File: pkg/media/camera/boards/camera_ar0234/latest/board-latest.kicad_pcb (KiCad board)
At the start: 6 copper layers, 32 x 32 mm, 69 parts, among them J1 FH34SRJ-22S-0.5SH_50_, Q1 BSS138, Q2 BSS138, U2 ATtiny402-SS, U3 LP5907MFX-2.8, U4 TLV74318PDBVR, U5 TLV75512PDYDR, X1 ECS-2520MV-240-DN-TR

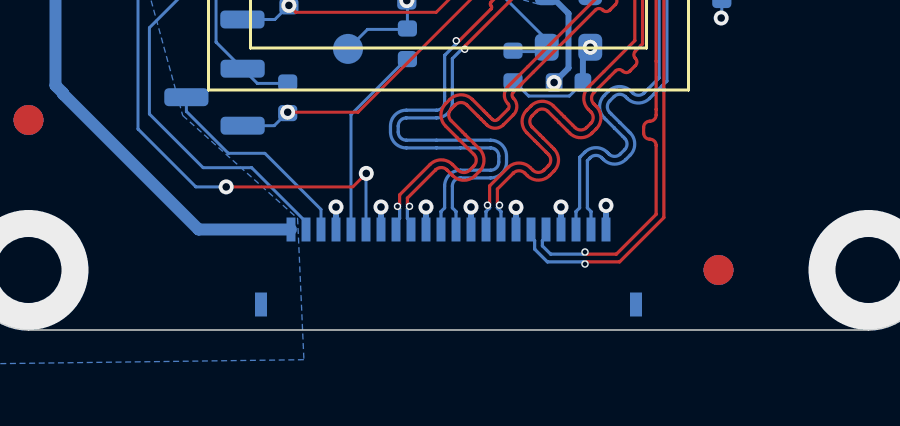
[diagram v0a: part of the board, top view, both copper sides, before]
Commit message: Adding more cnc logging logic.
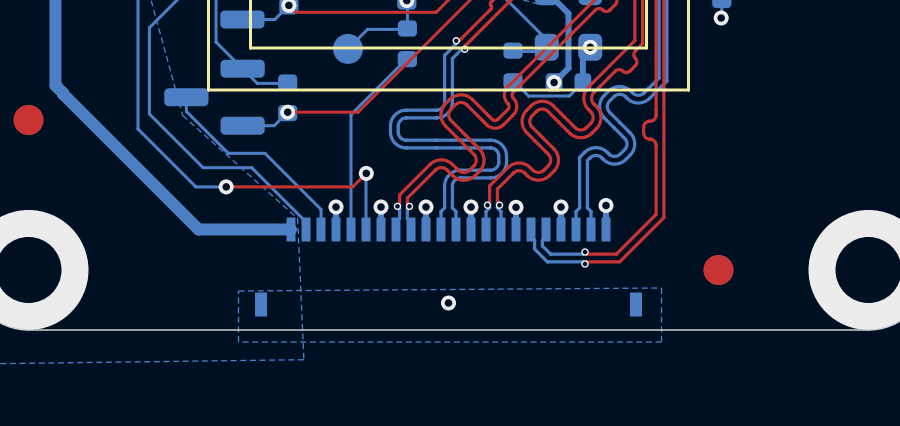
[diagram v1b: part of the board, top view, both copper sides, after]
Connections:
- J1 pad S1: unconnected-(J1-SHIELD-PadS1)_1 -> GND
- J1 pad S2: unconnected-(J1-SHIELD-PadS1) -> GND
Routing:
- net GND: vias 45 -> 46

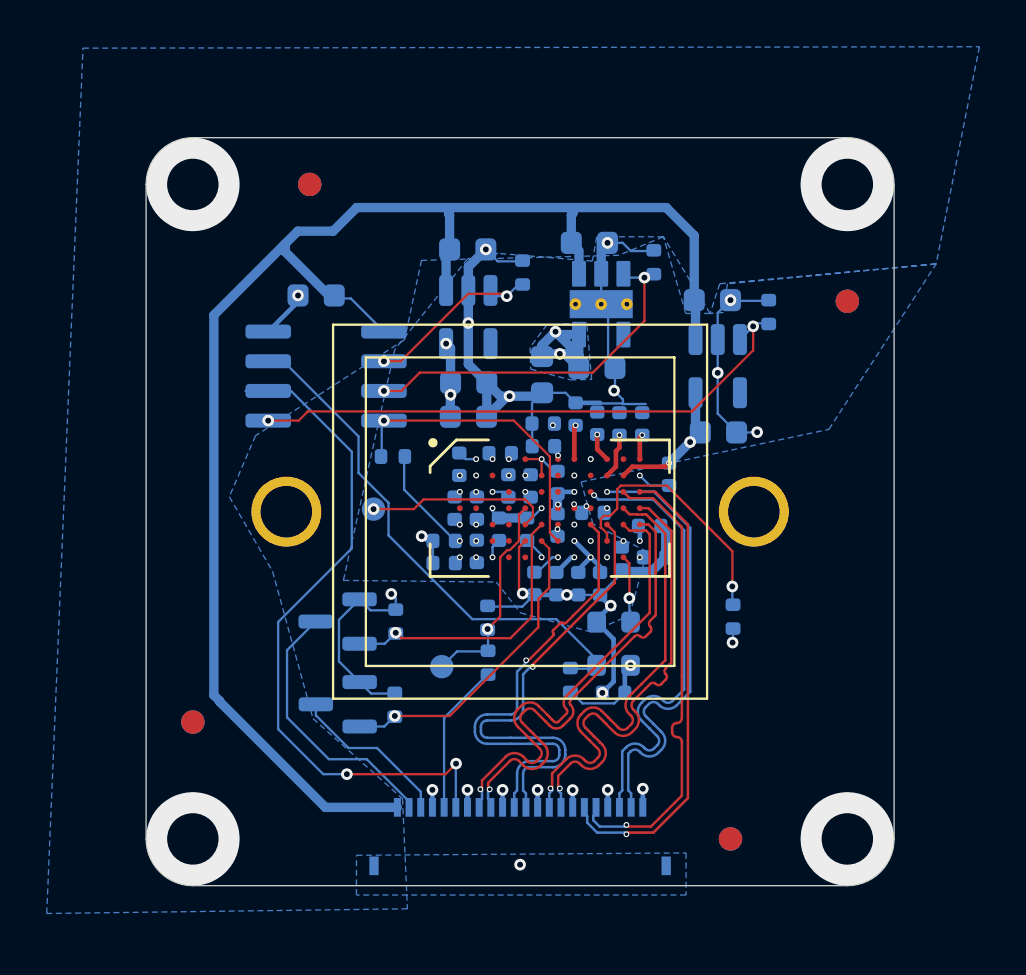
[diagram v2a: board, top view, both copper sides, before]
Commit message: Mocap tweaks and add CM4 support with SDCard.
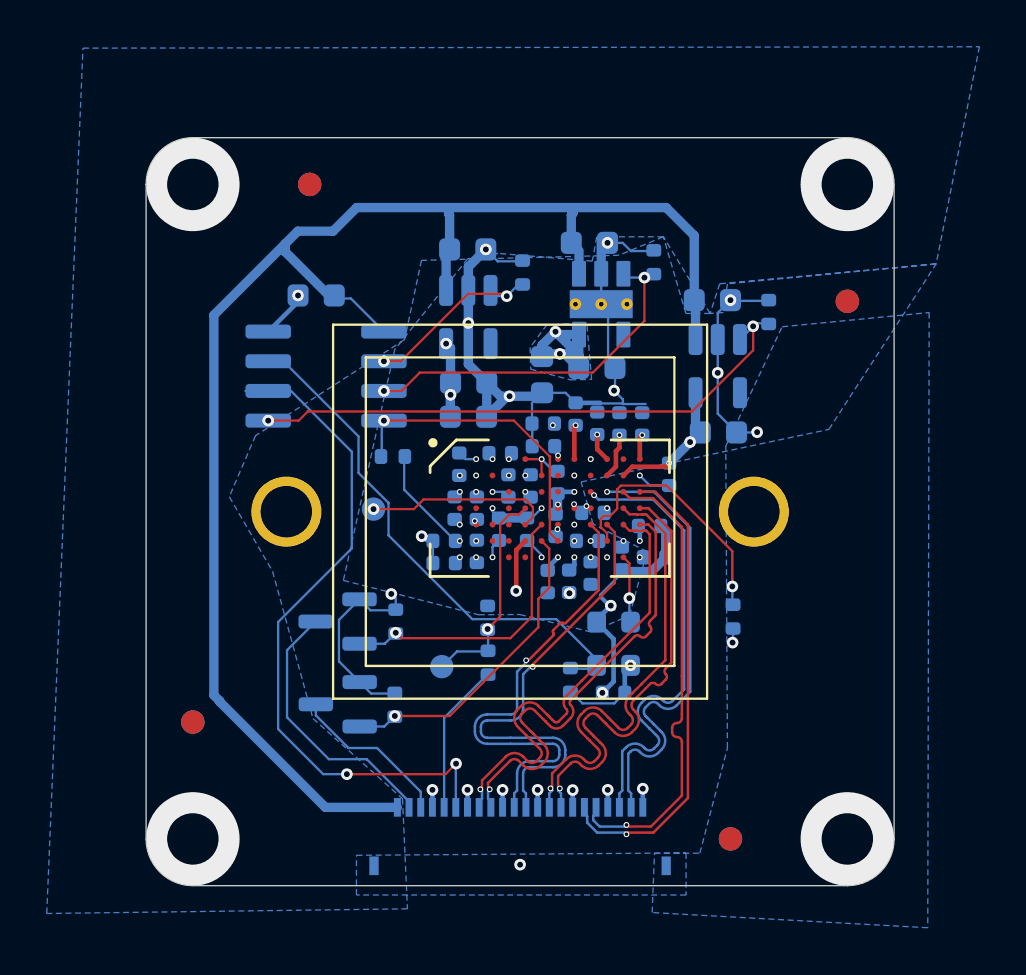
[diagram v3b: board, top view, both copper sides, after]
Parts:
- U3: value LP5907MFX-2.8 -> NCP163ASN280T1G
- moved C1 1.91 mm to (118.9, 117.2), turned to 0 degrees
- moved C9 0.70 mm to (119.0, 118.6)
- moved C5 0.58 mm to (117.2, 119.0)
- moved C26 0.56 mm to (118.1, 119.0)
- moved C25 0.08 mm to (117.5, 116.6)
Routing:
- net GND: track 75.9 -> 70.2 mm
- net +2V8: track 35.6 -> 32.4 mm
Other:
- board text added: "AR0234 R2"
- board text removed: "AR R1"
